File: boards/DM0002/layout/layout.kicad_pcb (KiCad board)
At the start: 4 copper layers, 15 x 48.1 mm, 70 parts, among them J1 FTSH-105-01-L-DV-K-A, J2 USB4105-GF-A, SW1 KMR231G LFS, U1 TLV75801PDRVR, U2 W25Q16JVUXIQ, U3 RP2040, U4 SG-210STF 12.0000ML0, U5 TXB0102DCUR, U6 TXB0102DCUR, U7 TLV9001IDBVR

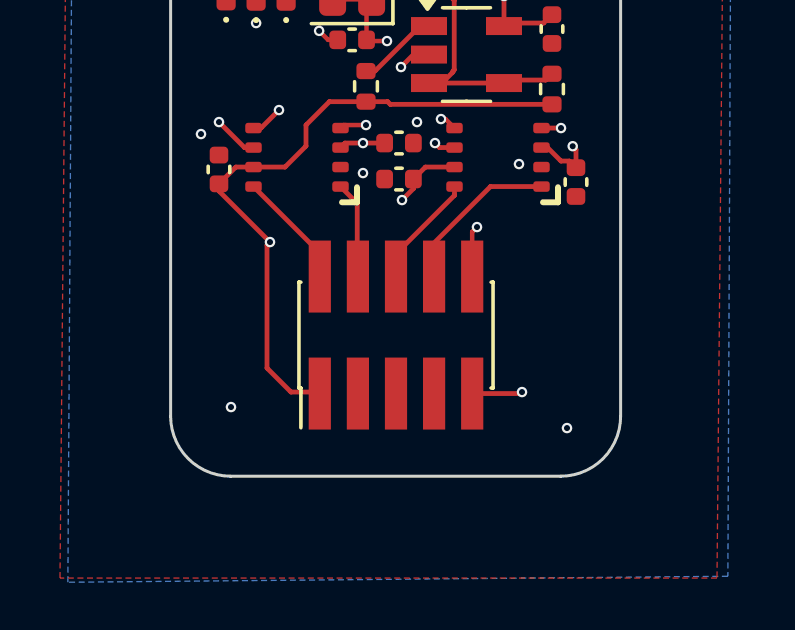
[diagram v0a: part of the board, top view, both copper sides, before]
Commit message: changed target header to one that has 3d model to show target mechanical keying
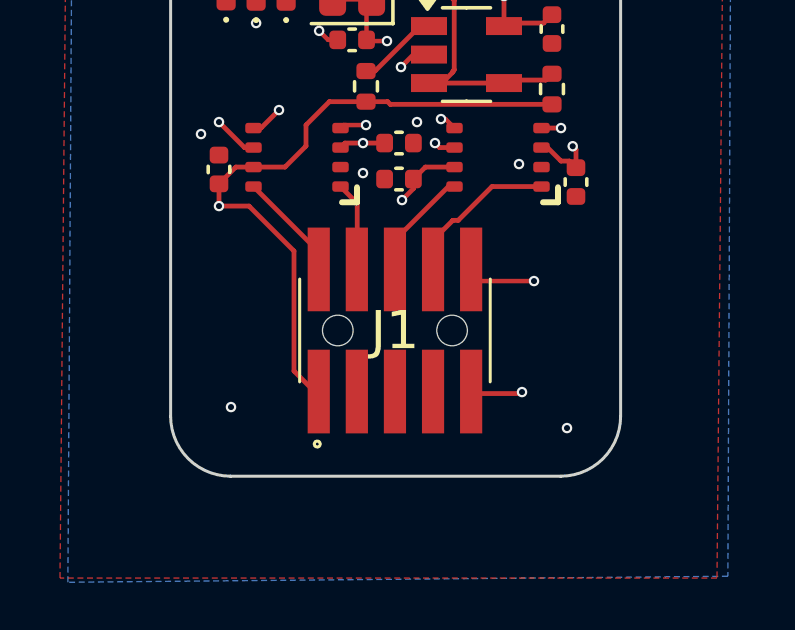
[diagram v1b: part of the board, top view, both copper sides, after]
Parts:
- J1: value FTSH-105-01-L-DV-K-A -> FTSH-105-01-L-DV-K-A-P-TR; footprint FTSH-105-01-L-DV-K-A:FTSH-105-01-L-DV-K-A -> FTSH-105-01-L-DV-K-A-P-TR:FTSH-105-01-L-DV-K-A-P-TR
- moved TP1 0.30 mm to (46.2, 86.7)
- moved J1 0.16 mm to (40.4, 86.6), turned to 0 degrees
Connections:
- net SWD_HEADER.NC_FTSH-105-01-L-DV-K-A_P7 renamed SWD_HEADER.NC_FTSH-105-01-L-DV-K-A-P-TR_7
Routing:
- net TARGET_VDDIO: track 29.1 -> 30.5 mm

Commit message: pre-gym commit
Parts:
- moved R18 17.5 mm to (47.0, 84.0), turned to 180 degrees
- moved R17 9.83 mm to (34.5, 80.0), turned to -90 degrees
- moved C3 1.30 mm to (47.5, 81.0)
- moved C2 0.70 mm to (34.5, 82.0), turned to -90 degrees
- moved C1 0.40 mm to (40.5, 80.0)
- moved C4 0.10 mm to (40.5, 81.5)
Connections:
- C1 pad 1: VDD_3V3 -> TARGET_VDDIO
- C2 pad 1: TARGET_VDDIO -> VDD_3V3
- C3 pad 1: VDD_3V3 -> TARGET_VDDIO
- C4 pad 1: TARGET_VDDIO -> VDD_3V3
- R17 pad 1: VDD_3V3 -> TARGET_VDDIO
- R18 pad 1: VDD_3V3 -> TARGET_VDDIO
- U3 pad 13: SWD_LS_OE -> MCU.GPIO10
- U3 pad 14: UART_LS_OE -> MCU.GPIO11
- U5 pad 1: SWD_SWCLK -> MCU_SWCLK
- U5 pad 3: VDD_3V3 -> TARGET_VDDIO
- U5 pad 4: MCU_SWCLK -> SWD_SWCLK
- U5 pad 5: MCU_SWDIO -> SWD_SWDIO
- U5 pad 7: TARGET_VDDIO -> VDD_3V3
- U5 pad 8: SWD_SWDIO -> MCU_SWDIO
- U6 pad 1: TARGET_UART_TX -> MCU_UART_TX
- U6 pad 3: VDD_3V3 -> TARGET_VDDIO
- U6 pad 4: MCU_UART_TX -> TARGET_UART_TX
- U6 pad 5: MCU_UART_RX -> TARGET_UART_RX
- U6 pad 7: TARGET_VDDIO -> VDD_3V3
- U6 pad 8: TARGET_UART_RX -> MCU_UART_RX
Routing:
- net TARGET_VDDIO: track 30.5 -> 6.99 mm, vias 2 -> 0
- net UART_LS_OE: track 21.5 -> 0.83 mm, vias 2 -> 1
- net SWD_LS_OE: track 15.1 -> 1.16 mm, vias 2 -> 0
- net TARGET_UART_RX: track 3.20 -> 8.05 mm
- net GND: track 36.6 -> 40.4 mm, vias 30 -> 27
- net SWD_SWCLK: track 2.50 -> 6.07 mm
- net MCU_SWCLK: track 13.5 -> 16.7 mm
- net SWD_SWDIO: track 3.17 -> 6.13 mm
- net TARGET_UART_TX: track 4.83 -> 7.64 mm
- net VDD_3V3: track 48.9 -> 46.2 mm, vias 15 -> 13
- net MCU_UART_TX: track 16.2 -> 18.8 mm
- net MCU_SWDIO: track 16.9 -> 18.4 mm
- net MCU_UART_RX: track 17.5 -> 18.9 mm

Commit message: level shift ports fixed, routing redone
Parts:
- moved R18 7.39 mm to (40.5, 80.5), turned to 0 degrees
- moved C3 1.00 mm to (46.5, 81.0)
- moved R19 0.65 mm to (39.0, 78.0), turned to 0 degrees
- moved C1 0.50 mm to (40.5, 79.5)
- moved C2 0.50 mm to (35.0, 82.0)
- moved R17 0.50 mm to (35.0, 80.0)
- moved U5 0.40 mm to (37.5, 80.9)
- moved C4 0.12 mm to (40.5, 81.6)
- moved R16 0.10 mm to (45.5, 78.6)
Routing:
- net TARGET_VDDIO: track 6.99 -> 40.3 mm, vias 0 -> 2
- net VDD_3V3: track 46.2 -> 56.3 mm, vias 13 -> 15
- net GND: track 40.4 -> 38.2 mm, vias 27 -> 31
- net UART_LS_OE: track 0.83 -> 1.37 mm, vias 1 -> 0
